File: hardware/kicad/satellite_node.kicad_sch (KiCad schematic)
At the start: 4 parts, among them U1 Seeed Studio XIAO ESP32S3, U2 SmartElex KX134-1211 (acceler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, U3 INMP441 (I2S microphone), U4 WS2812B x8 status ring

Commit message: schematics: name controller pins the way the boards name them
The three KiCad schematics labelled every controller pin by its MCU function
or STM32 port -- SCK, MISO, I2S_CLK, LED_DIN, PB0 -- which is not what any of
these boards is silkscreened with and not what you plug a wire into. Someone
holding an UNO Q and the schematic had no way to find "I2S_CLK".

Pins now carry the board's own header labels: D13/D12/D11/D8/D9/SCL/D10/A4/D3
on the UNO Q, D0-D10 on the XIAO, D2-D8 on the Uno under the CNC shield. The
signal's role moves into the net label, where it was already half-living
(SPI_SCK_D13, MIC_SD_A4), so each sensor stub still says both what the line
carries and which header pin it lands on. Sensor and driver symbols keep
their datasheet names -- those breakouts really are marked SCK/SDO/STEP.

Two labels were also just wrong, not merely inconvenient: the ring's DIN read
LED_DIN_PB0 when PB0 is header pin D3, and the mic's three lines read
PB10/PB9/PC1 with no header pin at all -- they are SCL, D10 and A4. Mapping is
the board's own gpio-map (arduino_r3_connector.dtsi) for the UNO Q and
board_pins.h for the XIAO; the mic's bit clock is genuinely the odd one out,
since PB10 comes out as the dedicated SCL pin rather than a D-number.

Appendix B.1's table gains the same treatment, and the report PNGs are
re-cropped to the drawing rather than the sheet -- they were carrying about
half a page of blank paper each, which shrank the schematic on the page. The
crop is now derived in the README instead of living in shell history.

Co-Authored-By: Claude Opus 5 <noreply@anthropic.com>
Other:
- note added: "Report ref: Chapter 3.3 / Appendix B.2. XIAO pins are named by its own D0-D10 breakout labels -- not by GPIO number."
- note added: "Seeed Studio XIAO ESP32S3. Same sensor set as the base station, on the XIAO's 11 breakout GPIOs. No LED matrix here -- the ring alone carries status."
- note removed: "Report ref: Chapter 3.3 / Appendix B.2. No LED matrix on this node -- the ring alone carries status."
- note removed: "Seeed Studio XIAO ESP32S3. Same sensor set as the base station, wired to the XIAO's 11 breakout GPIOs."
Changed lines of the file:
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@@
 		(effects (font (size 3.0 3.0)) (justify left))
 	)
-	(text "Seeed Studio XIAO ESP32S3. Same sensor set as the base station, wired to the XIAO's 11 breakout GPIOs."
+	(text "Seeed Studio XIAO ESP32S3. Same sensor set as the base station, on the XIAO's 11 breakout GPIOs. No LED matrix here -- the ring alone carries status."
 		(exclude_from_sim no)
 		(at 20 32 0)
 		(effects (font (size 1.8 1.8)) (justify left))
 	)
-	(text "Report ref: Chapter 3.3 / Appendix B.2. No LED matrix on this node -- the ring alone carries status."
+	(text "Report ref: Chapter 3.3 / Appendix B.2. XIAO pins are named by its own D0-D10 breakout labels -- not by GPIO number."
 		(exclude_from_sim no)
 		(at 20 38 0)
@@
 		(instances
 			(project "epm"
-				(path "/04a85245-000d-4b3e-9b55-3f19b2d83d0a"
+				(path "/1020049a-b7c6-4550-8e35-872c584c4f1e"
 					(reference "U1")
 					(unit 1)
@@
 		(on_board yes)
 		(dnp no)
-		(property "Reference" "#PWRa255"
+		(property "Reference" "#PWR0404"
 			(at 94.29 118.41499999999999 0)
 			(effects (font (size 1.27 1.27)) (hide yes))
@@
 		(instances
 			(project "epm"
-				(path "/04a85245-000d-4b3e-9b55-3f19b2d83d0a"
-					(reference "#PWRa255")
+				(path "/1020049a-b7c6-4550-8e35-872c584c4f1e"
+					(reference "#PWR0404")
 					(unit 1)
 				)
@@
 		(on_board yes)
 		(dnp no)
-		(property "Reference" "#PWR2a2a"
+		(property "Reference" "#PWRc746"
 			(at 94.29 124.76499999999999 0)
 			(effects (font (size 1.27 1.27)) (hide yes))
@@
 		(instances
 			(project "epm"
-				(path "/04a85245-000d-4b3e-9b55-3f19b2d83d0a"
-					(reference "#PWR2a2a")
+				(path "/1020049a-b7c6-4550-8e35-872c584c4f1e"
+					(reference "#PWRc746")
 					(unit 1)
 				)
@@
 		(on_board yes)
 		(dnp no)
-		(property "Reference" "#PWR6683"
+		(property "Reference" "#PWR0620"
 			(at 94.29 131.115 0)
 			(effects (font (size 1.27 1.27)) (hide yes))
@@
 		(instances
 			(project "epm"
-				(path "/04a85245-000d-4b3e-9b55-3f19b2d83d0a"
-					(reference "#PWR6683")
+				(path "/1020049a-b7c6-4550-8e35-872c584c4f1e"
+					(reference "#PWR0620")
 					(unit 1)
 				)
@@
 		(instances
 			(project "epm"
-				(path "/04a85245-000d-4b3e-9b55-3f19b2d83d0a"
+				(path "/1020049a-b7c6-4550-8e35-872c584c4f1e"
 					(reference "U2")
 					(unit 1)
@@
 		(on_board yes)
 		(dnp no)
-		(property "Reference" "#PWRe95e"
+		(property "Reference" "#PWR40f7"
 			(at 143.32999999999998 78.89 0)
 			(effects (font (size 1.27 1.27)) (hide yes))
@@
 		(instances
 			(project "epm"
-				(path "/04a85245-000d-4b3e-9b55-3f19b2d83d0a"
-					(reference "#PWRe95e")
+				(path "/1020049a-b7c6-4550-8e35-872c584c4f1e"
+					(reference "#PWR40f7")
 					(unit 1)
 				)
@@
 		(on_board yes)
 		(dnp no)
-		(property "Reference" "#PWR11ba"
+		(property "Reference" "#PWRb688"
 			(at 143.32999999999998 85.24 0)
 			(effects (font (size 1.27 1.27)) (hide yes))
@@
 		(instances
 			(project "epm"
-				(path "/04a85245-000d-4b3e-9b55-3f19b2d83d0a"
-					(reference "#PWR11ba")
+				(path "/1020049a-b7c6-4550-8e35-872c584c4f1e"
+					(reference "#PWRb688")
 					(unit 1)
 				)
@@
 		(instances
 			(project "epm"
-				(path "/04a85245-000d-4b3e-9b55-3f19b2d83d0a"
+				(path "/1020049a-b7c6-4550-8e35-872c584c4f1e"
 					(reference "U3")
 					(unit 1)
@@
 		(on_board yes)
 		(dnp no)
-		(property "Reference" "#PWR93be"
+		(property "Reference" "#PWR8ab2"
 			(at 144.60000000000002 124.36500000000001 0)
 			(effects (font (size 1.27 1.27)) (hide yes))
@@
 		(instances
 			(project "epm"
-				(path "/04a85245-000d-4b3e-9b55-3f19b2d83d0a"
-					(reference "#PWR93be")
+				(path "/1020049a-b7c6-4550-8e35-872c584c4f1e"
+					(reference "#PWR8ab2")
 					(unit 1)
 				)
@@
 		(on_board yes)
 		(dnp no)
-		(property "Reference" "#PWRbde2"
+		(property "Reference" "#PWR419d"
 			(at 144.60000000000002 130.715 0)
 			(effects (font (size 1.27 1.27)) (hide yes))
@@
 		(instances
 			(project "epm"
-				(path "/04a85245-000d-4b3e-9b55-3f19b2d83d0a"
-					(reference "#PWRbde2")
+				(path "/1020049a-b7c6-4550-8e35-872c584c4f1e"
+					(reference "#PWR419d")
 					(unit 1)
 				)
@@
 		(on_board yes)
 		(dnp no)
-		(property "Reference" "#PWR1e17"
+		(property "Reference" "#PWRee38"
 			(at 144.60000000000002 137.065 0)
 			(effects (font (size 1.27 1.27)) (hide yes))
@@
 		(instances
 			(project "epm"
-				(path "/04a85245-000d-4b3e-9b55-3f19b2d83d0a"
-					(reference "#PWR1e17")
+				(path "/1020049a-b7c6-4550-8e35-872c584c4f1e"
+					(reference "#PWRee38")
 					(unit 1)
 				)
@@
 		(instances
 			(project "epm"
-				(path "/04a85245-000d-4b3e-9b55-3f19b2d83d0a"
+				(path "/1020049a-b7c6-4550-8e35-872c584c4f1e"
 					(reference "U4")
 					(unit 1)
@@
 		(on_board yes)
 		(dnp no)
-		(property "Reference" "#PWRd9fe"
+		(property "Reference" "#PWRc592"
 			(at 144.60000000000002 166.19 0)
 			(effects (font (size 1.27 1.27)) (hide yes))
@@
 		(instances
 			(project "epm"
-				(path "/04a85245-000d-4b3e-9b55-3f19b2d83d0a"
-					(reference "#PWRd9fe")
+				(path "/1020049a-b7c6-4550-8e35-872c584c4f1e"
+					(reference "#PWRc592")
 					(unit 1)
 				)
@@
 		(on_board yes)
 		(dnp no)
-		(property "Reference" "#PWRc05d"
+		(property "Reference" "#PWR9a64"
 			(at 144.60000000000002 172.54 0)
 			(effects (font (size 1.27 1.27)) (hide yes))
@@
 		(instances
 			(project "epm"
-				(path "/04a85245-000d-4b3e-9b55-3f19b2d83d0a"
-					(reference "#PWRc05d")
-					(unit 1)
-				)
+				(path "/1020049a-b7c6-4550-8e35-872c584c4f1e"
+					(reference "#PWR9a64")
+					(unit 1)
+				)

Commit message: schematics: drop redundant pin-number suffix from net labels
The symbol pin already shows the pin number (D8, A4, SCL, ...), so
repeating it in the net label (SPI_SCK_D8) was noise. Net labels now
carry only the signal role (SPI_SCK, MIC_SD, ENABLE, ...).

Co-Authored-By: Claude Sonnet 5 <noreply@anthropic.com>
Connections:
- net ACC_CS_D3 renamed ACC_CS
- net ACC_INT_D2 renamed ACC_INT
- net LED_DIN_D5 renamed LED_DIN
- net MIC_SCK_D1 renamed MIC_SCK
- net MIC_SD_D4 renamed MIC_SD
- net MIC_WS_D0 renamed MIC_WS
- net SPI_MISO_D9 renamed SPI_MISO
- net SPI_MOSI_D10 renamed SPI_MOSI
- net SPI_SCK_D8 renamed SPI_SCK
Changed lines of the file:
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@@
 		(stroke (width 0) (type default))
 	)
-	(label "SPI_SCK_D8"
+	(label "SPI_SCK"
 		(at 94.29 65.075 0)
 		(effects (font (size 1.27 1.27)) (justify left))
 	)
-	(label "SPI_MISO_D9"
+	(label "SPI_MISO"
 		(at 94.29 71.425 0)
 		(effects (font (size 1.27 1.27)) (justify left))
 	)
-	(label "SPI_MOSI_D10"
+	(label "SPI_MOSI"
 		(at 94.29 77.775 0)
 		(effects (font (size 1.27 1.27)) (justify left))
 	)
-	(label "ACC_CS_D3"
+	(label "ACC_CS"
 		(at 94.29 84.125 0)
 		(effects (font (size 1.27 1.27)) (justify left))
 	)
-	(label "ACC_INT_D2"
+	(label "ACC_INT"
 		(at 94.29 90.475 0)
 		(effects (font (size 1.27 1.27)) (justify left))
 	)
-	(label "MIC_WS_D0"
+	(label "MIC_WS"
 		(at 94.29 96.825 0)
 		(effects (font (size 1.27 1.27)) (justify left))
 	)
-	(label "MIC_SCK_D1"
+	(label "MIC_SCK"
 		(at 94.29 103.175 0)
 		(effects (font (size 1.27 1.27)) (justify left))
 	)
-	(label "MIC_SD_D4"
+	(label "MIC_SD"
 		(at 94.29 109.525 0)
 		(effects (font (size 1.27 1.27)) (justify left))
 	)
-	(label "LED_DIN_D5"
+	(label "LED_DIN"
 		(at 94.29 115.875 0)
 		(effects (font (size 1.27 1.27)) (justify left))
 	)
-	(label "SPI_SCK_D8"
+	(label "SPI_SCK"
 		(at 143.32999999999998 50.95 0)
 		(effects (font (size 1.27 1.27)) (justify right))
 	)
-	(label "SPI_MISO_D9"
+	(label "SPI_MISO"
 		(at 143.32999999999998 57.3 0)
 		(effects (font (size 1.27 1.27)) (justify right))
 	)
-	(label "SPI_MOSI_D10"
+	(label "SPI_MOSI"
 		(at 143.32999999999998 63.65 0)
 		(effects (font (size 1.27 1.27)) (justify right))
 	)
-	(label "ACC_CS_D3"
+	(label "ACC_CS"
 		(at 143.32999999999998 70.0 0)
 		(effects (font (size 1.27 1.27)) (justify right))
 	)
-	(label "ACC_INT_D2"
+	(label "ACC_INT"
 		(at 143.32999999999998 76.35 0)
 		(effects (font (size 1.27 1.27)) (justify right))
 	)
-	(label "MIC_SCK_D1"
+	(label "MIC_SCK"
 		(at 144.60000000000002 109.125 0)
 		(effects (font (size 1.27 1.27)) (justify right))
 	)
-	(label "MIC_WS_D0"
+	(label "MIC_WS"
 		(at 144.60000000000002 115.475 0)
 		(effects (font (size 1.27 1.27)) (justify right))
 	)
-	(label "MIC_SD_D4"
+	(label "MIC_SD"
 		(at 144.60000000000002 121.825 0)
 		(effects (font (size 1.27 1.27)) (justify right))
 	)
-	(label "LED_DIN_D5"
+	(label "LED_DIN"
 		(at 144.60000000000002 163.65 0)
 		(effects (font (size 1.27 1.27)) (justify right))
@@
 		(instances
 			(project "epm"
-				(path "/1020049a-b7c6-4550-8e35-872c584c4f1e"
+				(path "/1f7ee488-ad22-4fe2-9435-05c89148eaac"
 					(reference "U1")
 					(unit 1)
@@
 		(on_board yes)
 		(dnp no)
-		(property "Reference" "#PWR0404"
+		(property "Reference" "#PWR6839"
 			(at 94.29 118.41499999999999 0)
 			(effects (font (size 1.27 1.27)) (hide yes))
@@
 		(instances
 			(project "epm"
-				(path "/1020049a-b7c6-4550-8e35-872c584c4f1e"
-					(reference "#PWR0404")
+				(path "/1f7ee488-ad22-4fe2-9435-05c89148eaac"
+					(reference "#PWR6839")
 					(unit 1)
 				)
@@
 		(on_board yes)
 		(dnp no)
-		(property "Reference" "#PWRc746"
+		(property "Reference" "#PWRc99a"
 			(at 94.29 124.76499999999999 0)
 			(effects (font (size 1.27 1.27)) (hide yes))
@@
 		(instances
 			(project "epm"
-				(path "/1020049a-b7c6-4550-8e35-872c584c4f1e"
-					(reference "#PWRc746")
+				(path "/1f7ee488-ad22-4fe2-9435-05c89148eaac"
+					(reference "#PWRc99a")
 					(unit 1)
 				)
@@
 		(on_board yes)
 		(dnp no)
-		(property "Reference" "#PWR0620"
+		(property "Reference" "#PWR9f31"
 			(at 94.29 131.115 0)
 			(effects (font (size 1.27 1.27)) (hide yes))
@@
 		(instances
 			(project "epm"
-				(path "/1020049a-b7c6-4550-8e35-872c584c4f1e"
-					(reference "#PWR0620")
+				(path "/1f7ee488-ad22-4fe2-9435-05c89148eaac"
+					(reference "#PWR9f31")
 					(unit 1)
 				)
@@
 		(instances
 			(project "epm"
-				(path "/1020049a-b7c6-4550-8e35-872c584c4f1e"
+				(path "/1f7ee488-ad22-4fe2-9435-05c89148eaac"
 					(reference "U2")
 					(unit 1)
@@
 		(on_board yes)
 		(dnp no)
-		(property "Reference" "#PWR40f7"
+		(property "Reference" "#PWR862a"
 			(at 143.32999999999998 78.89 0)
 			(effects (font (size 1.27 1.27)) (hide yes))
@@
 		(instances
 			(project "epm"
-				(path "/1020049a-b7c6-4550-8e35-872c584c4f1e"
-					(reference "#PWR40f7")
+				(path "/1f7ee488-ad22-4fe2-9435-05c89148eaac"
+					(reference "#PWR862a")
 					(unit 1)
 				)
@@
 		(on_board yes)
 		(dnp no)
-		(property "Reference" "#PWRb688"
+		(property "Reference" "#PWR7354"
 			(at 143.32999999999998 85.24 0)
 			(effects (font (size 1.27 1.27)) (hide yes))
@@
 		(instances
 			(project "epm"
-				(path "/1020049a-b7c6-4550-8e35-872c584c4f1e"
-					(reference "#PWRb688")
+				(path "/1f7ee488-ad22-4fe2-9435-05c89148eaac"
+					(reference "#PWR7354")
 					(unit 1)
 				)
@@
 		(instances
 			(project "epm"
-				(path "/1020049a-b7c6-4550-8e35-872c584c4f1e"
+				(path "/1f7ee488-ad22-4fe2-9435-05c89148eaac"
 					(reference "U3")
 					(unit 1)
@@
 		(on_board yes)
 		(dnp no)
-		(property "Reference" "#PWR8ab2"
+		(property "Reference" "#PWR2e77"
 			(at 144.60000000000002 124.36500000000001 0)
 			(effects (font (size 1.27 1.27)) (hide yes))
@@
 		(instances
 			(project "epm"
-				(path "/1020049a-b7c6-4550-8e35-872c584c4f1e"
-					(reference "#PWR8ab2")
+				(path "/1f7ee488-ad22-4fe2-9435-05c89148eaac"
+					(reference "#PWR2e77")
 					(unit 1)
 				)
@@
 		(on_board yes)
 		(dnp no)
-		(property "Reference" "#PWR419d"
+		(property "Reference" "#PWR3c21"
 			(at 144.60000000000002 130.715 0)
 			(effects (font (size 1.27 1.27)) (hide yes))
@@
 		(instances
 			(project "epm"
-				(path "/1020049a-b7c6-4550-8e35-872c584c4f1e"
-					(reference "#PWR419d")
+				(path "/1f7ee488-ad22-4fe2-9435-05c89148eaac"
+					(reference "#PWR3c21")
 					(unit 1)
 				)
@@
 		(on_board yes)
 		(dnp no)
-		(property "Reference" "#PWRee38"
+		(property "Reference" "#PWR761b"
 			(at 144.60000000000002 137.065 0)
 			(effects (font (size 1.27 1.27)) (hide yes))
@@
 		(instances
 			(project "epm"
-				(path "/1020049a-b7c6-4550-8e35-872c584c4f1e"
-					(reference "#PWRee38")
+				(path "/1f7ee488-ad22-4fe2-9435-05c89148eaac"
+					(reference "#PWR761b")
 					(unit 1)
 				)
@@
 		(instances
 			(project "epm"
-				(path "/1020049a-b7c6-4550-8e35-872c584c4f1e"
+				(path "/1f7ee488-ad22-4fe2-9435-05c89148eaac"
 					(reference "U4")
 					(unit 1)
@@
 		(on_board yes)
 		(dnp no)
-		(property "Reference" "#PWRc592"
+		(property "Reference" "#PWR5e36"
 			(at 144.60000000000002 166.19 0)
 			(effects (font (size 1.27 1.27)) (hide yes))
@@
 		(instances
 			(project "epm"
-				(path "/1020049a-b7c6-4550-8e35-872c584c4f1e"
-					(reference "#PWRc592")
+				(path "/1f7ee488-ad22-4fe2-9435-05c89148eaac"
+					(reference "#PWR5e36")
 					(unit 1)
 				)
@@
 		(on_board yes)
 		(dnp no)
-		(property "Reference" "#PWR9a64"
+		(property "Reference" "#PWR55da"
 			(at 144.60000000000002 172.54 0)
 			(effects (font (size 1.27 1.27)) (hide yes))
@@
 		(instances
 			(project "epm"
-				(path "/1020049a-b7c6-4550-8e35-872c584c4f1e"
-					(reference "#PWR9a64")
-					(unit 1)
-				)
+				(path "/1f7ee488-ad22-4fe2-9435-05c89148eaac"
+					(reference "#PWR55da")
+					(unit 1)
+				)

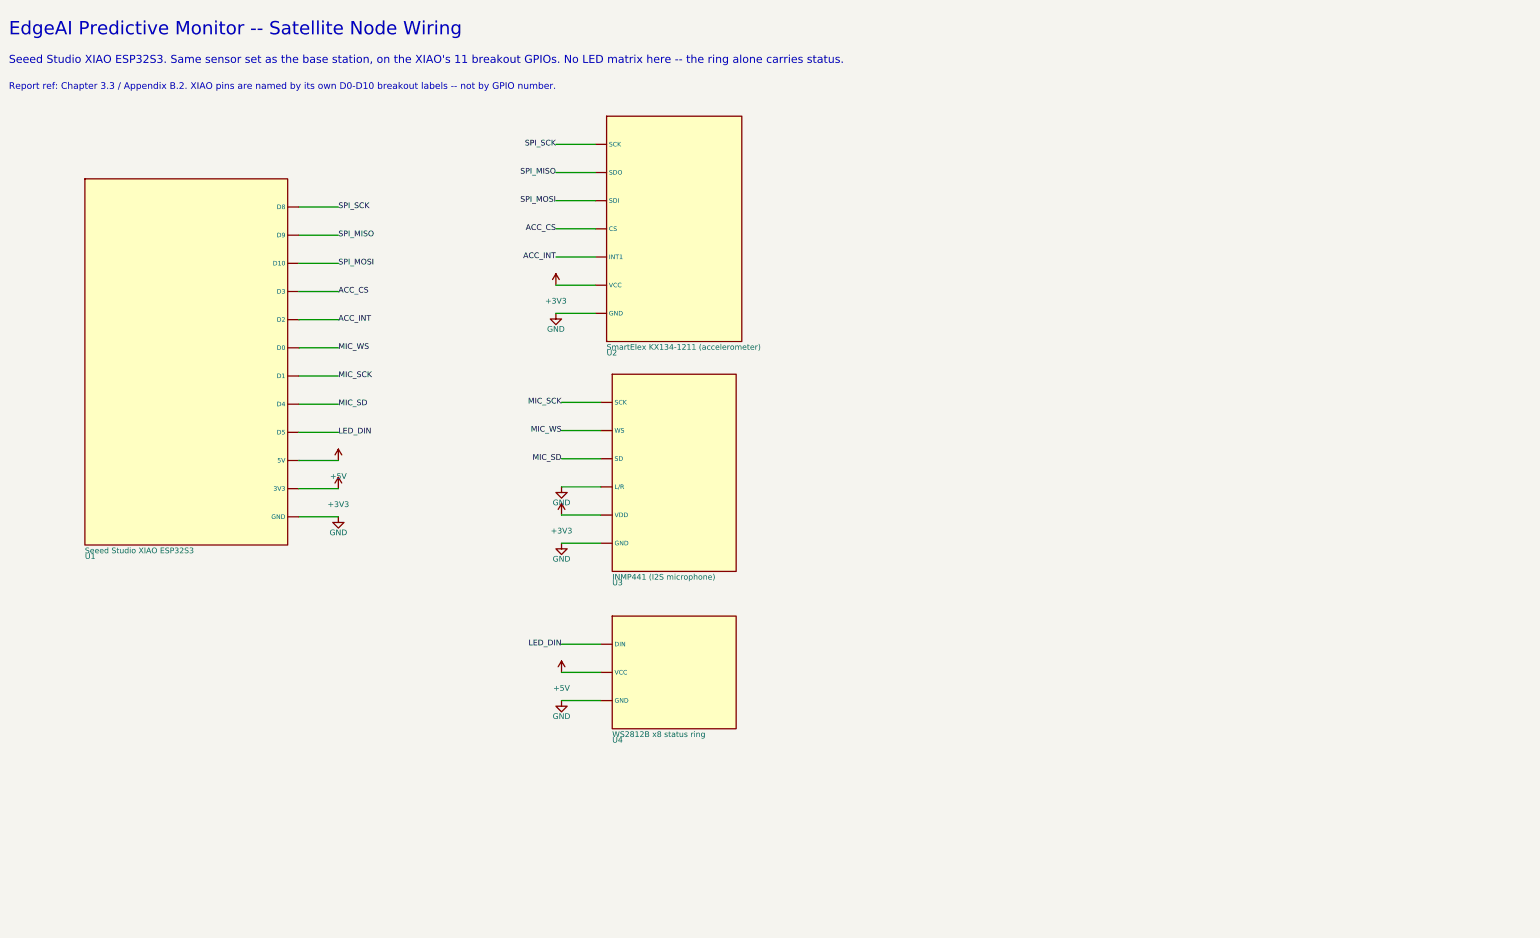
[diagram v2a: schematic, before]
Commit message: schematics: drop report-ref line, enlarge text, tighten crop
The report ref (Chapter/Appendix) was tied to a report structure the
submitted template doesn't use, so it's gone -- the useful pin-naming
and trimpot notes it was bundled with stayed. Separately, headings,
pin names, and net labels were too small to read once pasted into a
Word doc, so all text sizes went up in gen.py; row spacing now derives
from each part's real box height (via a new stack_column() helper)
instead of fixed y-coordinates, since the bigger fonts no longer fit
the old hand-picked positions. Crop step now masks out just the
title-block corner instead of scanning a fixed window, which cuts the
white margin around each exported PNG/PDF down to ~25px.

Co-Authored-By: Claude Sonnet 5 <noreply@anthropic.com>
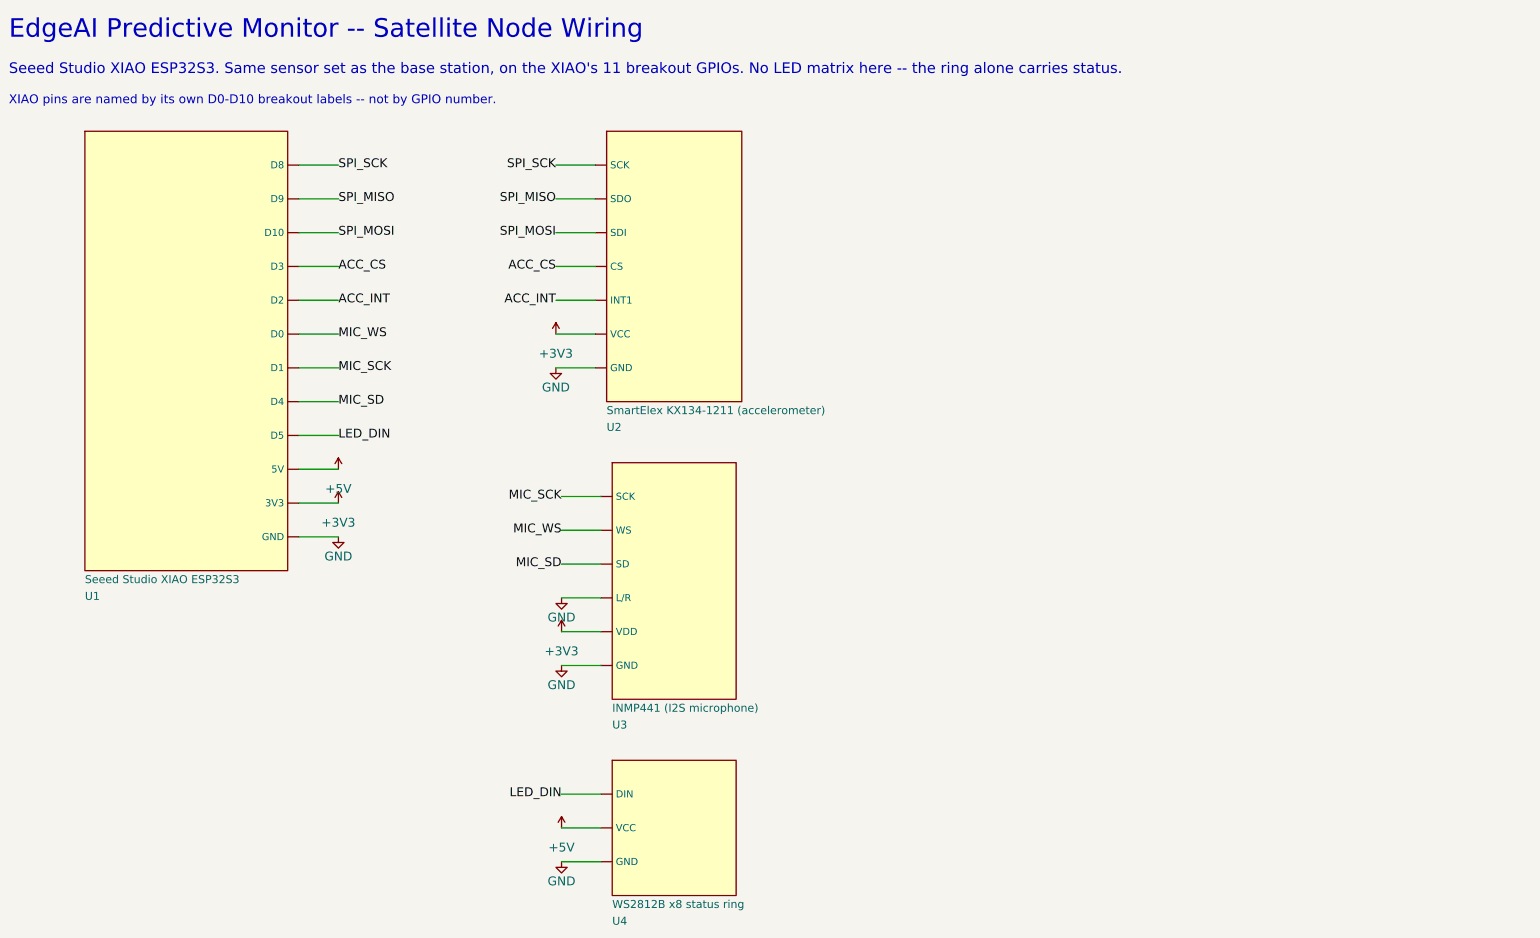
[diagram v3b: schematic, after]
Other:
- note added: "XIAO pins are named by its own D0-D10 breakout labels -- not by GPIO number."
- note removed: "Report ref: Chapter 3.3 / Appendix B.2. XIAO pins are named by its own D0-D10 breakout labels -- not by GPIO number."
